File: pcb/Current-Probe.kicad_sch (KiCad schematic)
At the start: 9 parts, among them J1 M1, J2 M2, J3 IN, J4 OUT

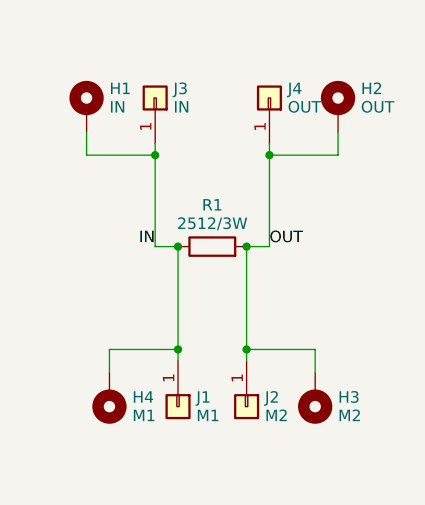
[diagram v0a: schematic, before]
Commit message: style: renumber the connectors
The different number order between the two connector sets triggered me...
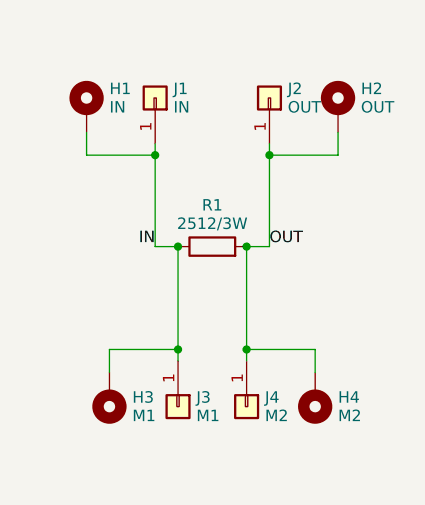
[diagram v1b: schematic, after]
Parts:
- renumbered H4 to H3, H3 to H4, J3 to J1, J4 to J2, J1 to J3, J2 to J4
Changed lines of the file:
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@@
   (symbol (lib_id "Connector_Generic:Conn_01x01") (at 151.13 50.8 270) (mirror x) (unit 1)
     (in_bom yes) (on_board yes) (dnp no) (fields_autoplaced)
-    (property "Reference" "J4" (at 153.162 49.776 90)
+    (property "Reference" "J2" (at 153.162 49.776 90)
       (effects (font (size 1.27 1.27)) (justify left))
     )
@@
       (project "Current-Probe"
         (path "/bc039c2a-6aaf-4e79-943f-f84ce3a9a58e"
+          (reference "J2") (unit 1)
+        )
+      )
+    )
+  )
+  (symbol (lib_id "Connector_Generic:Conn_01x01") (at 140.97 85.09 270) (unit 1)
+    (in_bom yes) (on_board yes) (dnp no) (fields_autoplaced)
+    (property "Reference" "J3" (at 143.002 84.066 90)
+      (effects (font (size 1.27 1.27)) (justify left))
+    )
+    (property "Value" "M1" (at 143.002 86.114 90)
+      (effects (font (size 1.27 1.27)) (justify left))
+    )
+    (property "Footprint" "My_Footprints:4mm_print_socket_with_hole" (at 140.97 85.09 0)
+      (effects (font (size 1.27 1.27)) hide)
+    )
+    (property "Datasheet" "~" (at 140.97 85.09 0)
+      (effects (font (size 1.27 1.27)) hide)
+    )
+    (pin "1")
+    (instances
+      (project "Current-Probe"
+        (path "/bc039c2a-6aaf-4e79-943f-f84ce3a9a58e"
+          (reference "J3") (unit 1)
+        )
+      )
+    )
+  )
+  (symbol (lib_id "Connector_Generic:Conn_01x01") (at 138.43 50.8 270) (mirror x) (unit 1)
+    (in_bom yes) (on_board yes) (dnp no) (fields_autoplaced)
+    (property "Reference" "J1" (at 140.462 49.776 90)
+      (effects (font (size 1.27 1.27)) (justify left))
+    )
+    (property "Value" "IN" (at 140.462 51.824 90)
+      (effects (font (size 1.27 1.27)) (justify left))
+    )
+    (property "Footprint" "My_Footprints:4mm_print_socket_with_hole" (at 138.43 50.8 0)
+      (effects (font (size 1.27 1.27)) hide)
+    )
+    (property "Datasheet" "~" (at 138.43 50.8 0)
+      (effects (font (size 1.27 1.27)) hide)
+    )
+    (pin "1")
+    (instances
+      (project "Current-Probe"
+        (path "/bc039c2a-6aaf-4e79-943f-f84ce3a9a58e"
+          (reference "J1") (unit 1)
+        )
+      )
+    )
+  )
+  (symbol (lib_id "Mechanical:MountingHole_Pad") (at 158.75 52.07 0) (mirror y) (unit 1)
+    (in_bom yes) (on_board yes) (dnp no) (fields_autoplaced)
+    (property "Reference" "H2" (at 161.29 49.776 0)
+      (effects (font (size 1.27 1.27)) (justify right))
+    )
+    (property "Value" "OUT" (at 161.29 51.824 0)
+      (effects (font (size 1.27 1.27)) (justify right))
+    )
+    (property "Footprint" "MountingHole:MountingHole_3.2mm_M3_Pad_Via" (at 158.75 52.07 0)
+      (effects (font (size 1.27 1.27)) hide)
+    )
+    (property "Datasheet" "~" (at 158.75 52.07 0)
+      (effects (font (size 1.27 1.27)) hide)
+    )
+    (pin "1")
+    (instances
+      (project "Current-Probe"
+        (path "/bc039c2a-6aaf-4e79-943f-f84ce3a9a58e"
+          (reference "H2") (unit 1)
+        )
+      )
+    )
+  )
+  (symbol (lib_id "Connector_Generic:Conn_01x01") (at 148.59 85.09 270) (unit 1)
+    (in_bom yes) (on_board yes) (dnp no) (fields_autoplaced)
+    (property "Reference" "J4" (at 150.622 84.066 90)
+      (effects (font (size 1.27 1.27)) (justify left))
+    )
+    (property "Value" "M2" (at 150.622 86.114 90)
+      (effects (font (size 1.27 1.27)) (justify left))
+    )
+    (property "Footprint" "My_Footprints:4mm_print_socket_with_hole" (at 148.59 85.09 0)
+      (effects (font (size 1.27 1.27)) hide)
+    )
+    (property "Datasheet" "~" (at 148.59 85.09 0)
+      (effects (font (size 1.27 1.27)) hide)
+    )
+    (pin "1")
+    (instances
+      (project "Current-Probe"
+        (path "/bc039c2a-6aaf-4e79-943f-f84ce3a9a58e"
           (reference "J4") (unit 1)
         )
@@
     )
   )
-  (symbol (lib_id "Connector_Generic:Conn_01x01") (at 140.97 85.09 270) (unit 1)
-    (in_bom yes) (on_board yes) (dnp no) (fields_autoplaced)
-    (property "Reference" "J1" (at 143.002 84.066 90)
-      (effects (font (size 1.27 1.27)) (justify left))
-    )
-    (property "Value" "M1" (at 143.002 86.114 90)
-      (effects (font (size 1.27 1.27)) (justify left))
-    )
-    (property "Footprint" "My_Footprints:4mm_print_socket_with_hole" (at 140.97 85.09 0)
-      (effects (font (size 1.27 1.27)) hide)
-    )
-    (property "Datasheet" "~" (at 140.97 85.09 0)
-      (effects (font (size 1.27 1.27)) hide)
-    )
-    (pin "1")
-    (instances
-      (project "Current-Probe"
-        (path "/bc039c2a-6aaf-4e79-943f-f84ce3a9a58e"
-          (reference "J1") (unit 1)
-        )
-      )
-    )
-  )
-  (symbol (lib_id "Connector_Generic:Conn_01x01") (at 138.43 50.8 270) (mirror x) (unit 1)
-    (in_bom yes) (on_board yes) (dnp no) (fields_autoplaced)
-    (property "Reference" "J3" (at 140.462 49.776 90)
-      (effects (font (size 1.27 1.27)) (justify left))
-    )
-    (property "Value" "IN" (at 140.462 51.824 90)
-      (effects (font (size 1.27 1.27)) (justify left))
-    )
-    (property "Footprint" "My_Footprints:4mm_print_socket_with_hole" (at 138.43 50.8 0)
-      (effects (font (size 1.27 1.27)) hide)
-    )
-    (property "Datasheet" "~" (at 138.43 50.8 0)
-      (effects (font (size 1.27 1.27)) hide)
-    )
-    (pin "1")
-    (instances
-      (project "Current-Probe"
-        (path "/bc039c2a-6aaf-4e79-943f-f84ce3a9a58e"
-          (reference "J3") (unit 1)
-        )
-      )
-    )
-  )
-  (symbol (lib_id "Mechanical:MountingHole_Pad") (at 158.75 52.07 0) (mirror y) (unit 1)
-    (in_bom yes) (on_board yes) (dnp no) (fields_autoplaced)
-    (property "Reference" "H2" (at 161.29 49.776 0)
-      (effects (font (size 1.27 1.27)) (justify right))
-    )
-    (property "Value" "OUT" (at 161.29 51.824 0)
-      (effects (font (size 1.27 1.27)) (justify right))
-    )
-    (property "Footprint" "MountingHole:MountingHole_3.2mm_M3_Pad_Via" (at 158.75 52.07 0)
-      (effects (font (size 1.27 1.27)) hide)
-    )
-    (property "Datasheet" "~" (at 158.75 52.07 0)
-      (effects (font (size 1.27 1.27)) hide)
-    )
-    (pin "1")
-    (instances
-      (project "Current-Probe"
-        (path "/bc039c2a-6aaf-4e79-943f-f84ce3a9a58e"
-          (reference "H2") (unit 1)
-        )
-      )
-    )
-  )
-  (symbol (lib_id "Connector_Generic:Conn_01x01") (at 148.59 85.09 270) (unit 1)
-    (in_bom yes) (on_board yes) (dnp no) (fields_autoplaced)
-    (property "Reference" "J2" (at 150.622 84.066 90)
-      (effects (font (size 1.27 1.27)) (justify left))
-    )
-    (property "Value" "M2" (at 150.622 86.114 90)
-      (effects (font (size 1.27 1.27)) (justify left))
-    )
-    (property "Footprint" "My_Footprints:4mm_print_socket_with_hole" (at 148.59 85.09 0)
-      (effects (font (size 1.27 1.27)) hide)
-    )
-    (property "Datasheet" "~" (at 148.59 85.09 0)
-      (effects (font (size 1.27 1.27)) hide)
-    )
-    (pin "1")
-    (instances
-      (project "Current-Probe"
-        (path "/bc039c2a-6aaf-4e79-943f-f84ce3a9a58e"
-          (reference "J2") (unit 1)
-        )
-      )
-    )
-  )
   (symbol (lib_id "Mechanical:MountingHole_Pad") (at 133.35 83.82 180) (unit 1)
     (in_bom yes) (on_board yes) (dnp no) (fields_autoplaced)
-    (property "Reference" "H4" (at 135.89 84.066 0)
+    (property "Reference" "H3" (at 135.89 84.066 0)
       (effects (font (size 1.27 1.27)) (justify right))
     )
@@
       (project "Current-Probe"
         (path "/bc039c2a-6aaf-4e79-943f-f84ce3a9a58e"
-          (reference "H4") (unit 1)
+          (reference "H3") (unit 1)
         )
       )
@@
   (symbol (lib_id "Mechanical:MountingHole_Pad") (at 156.21 83.82 180) (unit 1)
     (in_bom yes) (on_board yes) (dnp no) (fields_autoplaced)
-    (property "Reference" "H3" (at 158.75 84.066 0)
+    (property "Reference" "H4" (at 158.75 84.066 0)
       (effects (font (size 1.27 1.27)) (justify right))
     )
@@
       (project "Current-Probe"
         (path "/bc039c2a-6aaf-4e79-943f-f84ce3a9a58e"
-          (reference "H3") (unit 1)
-        )
-      )
+          (reference "H4") (unit 1)
+        )
+      )

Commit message: feat: add BNC connector
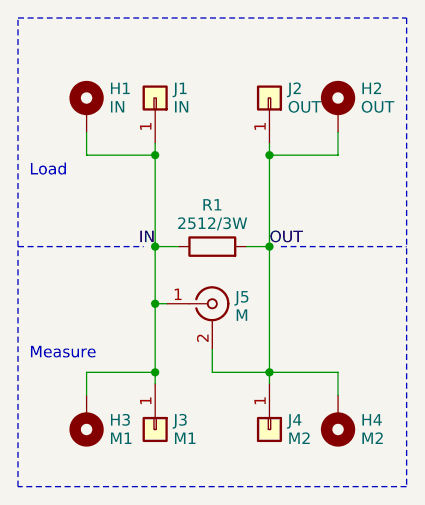
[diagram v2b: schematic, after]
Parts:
- added J5: M, Connector_Coaxial:BNC_TEConnectivity_1478204_Vertical, symbol Connector:Conn_Coaxial
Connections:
- net IN: now also J5.1 (In)
- net OUT: now also J5.2 (Ext)
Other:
- note added: "Load"
- note added: "Measure"
- moved on the sheet: H3, H4, J3, J4
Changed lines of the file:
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@@
     (rev "${VERSION}")
   )
+  (junction (at 151.13 81.28) (diameter 0) (color 0 0 0 0)
+  )
   (junction (at 138.43 57.15) (diameter 0) (color 0 0 0 0)
   )
-  (junction (at 140.97 78.74) (diameter 0) (color 0 0 0 0)
-  )
-  (junction (at 148.59 67.31) (diameter 0) (color 0 0 0 0)
-  )
-  (junction (at 148.59 78.74) (diameter 0) (color 0 0 0 0)
+  (junction (at 138.43 67.31) (diameter 0) (color 0 0 0 0)
+  )
+  (junction (at 151.13 67.31) (diameter 0) (color 0 0 0 0)
+  )
+  (junction (at 138.43 73.66) (diameter 0) (color 0 0 0 0)
   )
   (junction (at 151.13 57.15) (diameter 0) (color 0 0 0 0)
   )
-  (junction (at 140.97 67.31) (diameter 0) (color 0 0 0 0)
-  )
-  (wire (pts (xy 148.59 67.31) (xy 148.59 78.74))
+  (junction (at 138.43 81.28) (diameter 0) (color 0 0 0 0)
+  )
+  (wire (pts (xy 138.43 73.66) (xy 138.43 81.28))
     (stroke (width 0) (type default))
   )
@@
     (stroke (width 0) (type default))
   )
-  (wire (pts (xy 133.35 78.74) (xy 140.97 78.74))
+  (wire (pts (xy 130.81 81.28) (xy 138.43 81.28))
+    (stroke (width 0) (type default))
+  )
+  (polyline (pts (xy 123.19 67.31) (xy 137.16 67.31))
+    (stroke (width 0) (type dash))
+  )
+  (wire (pts (xy 138.43 73.66) (xy 139.7 73.66))
     (stroke (width 0) (type default))
   )
@@
     (stroke (width 0) (type default))
   )
-  (wire (pts (xy 140.97 67.31) (xy 140.97 78.74))
+  (wire (pts (xy 144.78 81.28) (xy 151.13 81.28))
     (stroke (width 0) (type default))
   )
@@
     (stroke (width 0) (type default))
   )
-  (wire (pts (xy 148.59 78.74) (xy 148.59 80.01))
+  (wire (pts (xy 138.43 67.31) (xy 138.43 73.66))
+    (stroke (width 0) (type default))
+  )
+  (wire (pts (xy 138.43 67.31) (xy 140.97 67.31))
+    (stroke (width 0) (type default))
+  )
+  (wire (pts (xy 151.13 81.28) (xy 151.13 82.55))
+    (stroke (width 0) (type default))
+  )
+  (wire (pts (xy 151.13 67.31) (xy 151.13 81.28))
+    (stroke (width 0) (type default))
+  )
+  (wire (pts (xy 144.78 81.28) (xy 144.78 78.74))
     (stroke (width 0) (type default))
   )
@@
     (stroke (width 0) (type default))
   )
-  (wire (pts (xy 138.43 67.31) (xy 140.97 67.31))
-    (stroke (width 0) (type default))
-  )
   (wire (pts (xy 151.13 55.88) (xy 151.13 57.15))
     (stroke (width 0) (type default))
@@
     (stroke (width 0) (type default))
   )
-  (wire (pts (xy 140.97 78.74) (xy 140.97 80.01))
+  (polyline (pts (xy 152.4 67.31) (xy 166.37 67.31))
+    (stroke (width 0) (type dash))
+  )
+  (wire (pts (xy 138.43 81.28) (xy 138.43 82.55))
     (stroke (width 0) (type default))
   )
@@
     (stroke (width 0) (type default))
   )
-  (wire (pts (xy 133.35 81.28) (xy 133.35 78.74))
-    (stroke (width 0) (type default))
-  )
-  (wire (pts (xy 156.21 81.28) (xy 156.21 78.74))
+  (wire (pts (xy 130.81 83.82) (xy 130.81 81.28))
+    (stroke (width 0) (type default))
+  )
+  (wire (pts (xy 158.75 83.82) (xy 158.75 81.28))
     (stroke (width 0) (type default))
   )
@@
     (stroke (width 0) (type default))
   )
-  (wire (pts (xy 156.21 78.74) (xy 148.59 78.74))
-    (stroke (width 0) (type default))
+  (wire (pts (xy 158.75 81.28) (xy 151.13 81.28))
+    (stroke (width 0) (type default))
+  )
+  (rectangle (start 123.19 41.91) (end 166.37 93.98)
+    (stroke (width 0) (type dash))
+    (fill (type none))
+  )
+  (text "Measure" (at 124.46 80.01 0)
+    (effects (font (size 1.27 1.27)) (justify left bottom))
+  )
+  (text "Load" (at 124.46 59.69 0)
+    (effects (font (size 1.27 1.27)) (justify left bottom))
   )
   (label "IN" (at 138.43 67.31 180) (fields_autoplaced)
@@
     )
   )
-  (symbol (lib_id "Connector_Generic:Conn_01x01") (at 140.97 85.09 270) (unit 1)
-    (in_bom yes) (on_board yes) (dnp no) (fields_autoplaced)
-    (property "Reference" "J3" (at 143.002 84.066 90)
-      (effects (font (size 1.27 1.27)) (justify left))
-    )
-    (property "Value" "M1" (at 143.002 86.114 90)
-      (effects (font (size 1.27 1.27)) (justify left))
-    )
-    (property "Footprint" "My_Footprints:4mm_print_socket_with_hole" (at 140.97 85.09 0)
-      (effects (font (size 1.27 1.27)) hide)
-    )
-    (property "Datasheet" "~" (at 140.97 85.09 0)
+  (symbol (lib_id "Connector_Generic:Conn_01x01") (at 138.43 87.63 270) (unit 1)
+    (in_bom yes) (on_board yes) (dnp no) (fields_autoplaced)
+    (property "Reference" "J3" (at 140.462 86.606 90)
+      (effects (font (size 1.27 1.27)) (justify left))
+    )
+    (property "Value" "M1" (at 140.462 88.654 90)
+      (effects (font (size 1.27 1.27)) (justify left))
+    )
+    (property "Footprint" "My_Footprints:4mm_print_socket_with_hole" (at 138.43 87.63 0)
+      (effects (font (size 1.27 1.27)) hide)
+    )
+    (property "Datasheet" "~" (at 138.43 87.63 0)
       (effects (font (size 1.27 1.27)) hide)
     )
@@
     )
   )
-  (symbol (lib_id "Connector_Generic:Conn_01x01") (at 148.59 85.09 270) (unit 1)
-    (in_bom yes) (on_board yes) (dnp no) (fields_autoplaced)
-    (property "Reference" "J4" (at 150.622 84.066 90)
-      (effects (font (size 1.27 1.27)) (justify left))
-    )
-    (property "Value" "M2" (at 150.622 86.114 90)
-      (effects (font (size 1.27 1.27)) (justify left))
-    )
-    (property "Footprint" "My_Footprints:4mm_print_socket_with_hole" (at 148.59 85.09 0)
-      (effects (font (size 1.27 1.27)) hide)
-    )
-    (property "Datasheet" "~" (at 148.59 85.09 0)
+  (symbol (lib_id "Connector_Generic:Conn_01x01") (at 151.13 87.63 270) (unit 1)
+    (in_bom yes) (on_board yes) (dnp no) (fields_autoplaced)
+    (property "Reference" "J4" (at 153.162 86.606 90)
+      (effects (font (size 1.27 1.27)) (justify left))
+    )
+    (property "Value" "M2" (at 153.162 88.654 90)
+      (effects (font (size 1.27 1.27)) (justify left))
+    )
+    (property "Footprint" "My_Footprints:4mm_print_socket_with_hole" (at 151.13 87.63 0)
+      (effects (font (size 1.27 1.27)) hide)
+    )
+    (property "Datasheet" "~" (at 151.13 87.63 0)
       (effects (font (size 1.27 1.27)) hide)
     )
@@
     )
   )
-  (symbol (lib_id "Mechanical:MountingHole_Pad") (at 133.35 83.82 180) (unit 1)
-    (in_bom yes) (on_board yes) (dnp no) (fields_autoplaced)
-    (property "Reference" "H3" (at 135.89 84.066 0)
-      (effects (font (size 1.27 1.27)) (justify right))
-    )
-    (property "Value" "M1" (at 135.89 86.114 0)
-      (effects (font (size 1.27 1.27)) (justify right))
-    )
-    (property "Footprint" "MountingHole:MountingHole_3.2mm_M3_Pad_Via" (at 133.35 83.82 0)
-      (effects (font (size 1.27 1.27)) hide)
-    )
-    (property "Datasheet" "~" (at 133.35 83.82 0)
+  (symbol (lib_id "Mechanical:MountingHole_Pad") (at 130.81 86.36 180) (unit 1)
+    (in_bom yes) (on_board yes) (dnp no) (fields_autoplaced)
+    (property "Reference" "H3" (at 133.35 86.606 0)
+      (effects (font (size 1.27 1.27)) (justify right))
+    )
+    (property "Value" "M1" (at 133.35 88.654 0)
+      (effects (font (size 1.27 1.27)) (justify right))
+    )
+    (property "Footprint" "MountingHole:MountingHole_3.2mm_M3_Pad_Via" (at 130.81 86.36 0)
+      (effects (font (size 1.27 1.27)) hide)
+    )
+    (property "Datasheet" "~" (at 130.81 86.36 0)
       (effects (font (size 1.27 1.27)) hide)
     )
@@
         (path "/bc039c2a-6aaf-4e79-943f-f84ce3a9a58e"
           (reference "H3") (unit 1)
+        )
+      )
+    )
+  )
+  (symbol (lib_id "Connector:Conn_Coaxial") (at 144.78 73.66 0) (unit 1)
+    (in_bom yes) (on_board yes) (dnp no) (fields_autoplaced)
+    (property "Reference" "J5" (at 147.3201 72.9292 0)
+      (effects (font (size 1.27 1.27)) (justify left))
+    )
+    (property "Value" "M" (at 147.3201 74.9772 0)
+      (effects (font (size 1.27 1.27)) (justify left))
+    )
+    (property "Footprint" "Connector_Coaxial:BNC_TEConnectivity_1478204_Vertical" (at 144.78 73.66 0)
+      (effects (font (size 1.27 1.27)) hide)
+    )
+    (property "Datasheet" " ~" (at 144.78 73.66 0)
+      (effects (font (size 1.27 1.27)) hide)
+    )
+    (pin "1")
+    (pin "2")
+    (instances
+      (project "Current-Probe"
+        (path "/bc039c2a-6aaf-4e79-943f-f84ce3a9a58e"
+          (reference "J5") (unit 1)
         )
       )
@@
     )
   )
-  (symbol (lib_id "Mechanical:MountingHole_Pad") (at 156.21 83.82 180) (unit 1)
-    (in_bom yes) (on_board yes) (dnp no) (fields_autoplaced)
-    (property "Reference" "H4" (at 158.75 84.066 0)
-      (effects (font (size 1.27 1.27)) (justify right))
-    )
-    (property "Value" "M2" (at 158.75 86.114 0)
-      (effects (font (size 1.27 1.27)) (justify right))
-    )
-    (property "Footprint" "MountingHole:MountingHole_3.2mm_M3_Pad_Via" (at 156.21 83.82 0)
-      (effects (font (size 1.27 1.27)) hide)
-    )
-    (property "Datasheet" "~" (at 156.21 83.82 0)
-      (effects (font (size 1.27 1.27)) hide)
-    )
+  (symbol (lib_id "Mechanical:MountingHole_Pad") (at 158.75 86.36 180) (unit 1)
+    (in_bom yes) (on_board yes) (dnp no) (fields_autoplaced)
+    (property "Reference" "H4" (at 161.29 86.606 0)
+      (effects (font (size 1.27 1.27)) (justify right))
+    )
+    (property "Value" "M2" (at 161.29 88.654 0)
+      (effects (font (size 1.27 1.27)) (justify right))
+    )
+    (property "Footprint" "MountingHole:MountingHole_3.2mm_M3_Pad_Via" (at 158.75 86.36 0)
+      (effects (font (size 1.27 1.27)) hide)
+    )
+    (property "Datasheet" "~" (at 158.75 86.36 0)
+      (effects (font (size 1.27 1.27)) hide)
+    )

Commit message: feat: remove 4mm sockets on measuring side
These were not needed anymore since the board will just be used with an oscilloscope anyway. The BNC connector does the job perfectly fine...
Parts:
- removed J3: M1, My_Footprints:4mm_print_socket_with_hole, symbol Connector_Generic:Conn_01x01
- removed J4: M2, My_Footprints:4mm_print_socket_with_hole, symbol Connector_Generic:Conn_01x01
- J3: renamed from J5; footprint Connector_Coaxial:BNC_TEConnectivity_1478204_Vertical -> Connector_Coaxial:BNC_Amphenol_B6252HB-NPP3G-50_Horizontal
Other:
- moved on the sheet: H3, H4
